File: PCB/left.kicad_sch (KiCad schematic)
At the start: 46 parts

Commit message: update footpint
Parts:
- D1, D10, D11, D12, D13, D14, D15, D16, D17, D18, D19, D2, D20, D21, D3, D4, D5, D6, D7, D8, D9: footprint kometa:Diode -> kometa:D_SOD323
- PS_L1: footprint kometa:MSK-12C02 -> kometa:SW_MSK-12C02
- PW_L1: footprint kometa:Battery -> kometa:J_Battery
- R_L1: footprint kometa:Reset -> kometa:SW_TS342A2P
- SM_L1: footprint kometa:SuperMini -> kometa:U_ProMicro_nRF52840
- SW1, SW10, SW11, SW12, SW13, SW14, SW15, SW16, SW17, SW18, SW19, SW2, SW20, SW21, SW3, SW4, SW5, SW6, SW7, SW8, SW9: footprint kometa:ChocV2 -> kometa:SW_Hotswap_Kailh_Choc_V1V2
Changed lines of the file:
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@@
 			)
 		)
-		(property "Footprint" "kometa:ChocV2"
+		(property "Footprint" "kometa:SW_Hotswap_Kailh_Choc_V1V2"
 			(at 79.756 105.41 0)
 			(effects
@@
 			)
 		)
-		(property "Footprint" "kometa:ChocV2"
+		(property "Footprint" "kometa:SW_Hotswap_Kailh_Choc_V1V2"
 			(at 136.906 105.41 0)
 			(effects
@@
 			)
 		)
-		(property "Footprint" "kometa:ChocV2"
+		(property "Footprint" "kometa:SW_Hotswap_Kailh_Choc_V1V2"
 			(at 41.656 86.36 0)
 			(effects
@@
 			)
 		)
-		(property "Footprint" "kometa:Diode"
+		(property "Footprint" "kometa:D_SOD323"
 			(at 138.176 102.362 0)
 			(effects
@@
 			)
 		)
-		(property "Footprint" "kometa:ChocV2"
+		(property "Footprint" "kometa:SW_Hotswap_Kailh_Choc_V1V2"
 			(at 136.906 86.36 0)
 			(effects
@@
 			)
 		)
-		(property "Footprint" "kometa:Diode"
+		(property "Footprint" "kometa:D_SOD323"
 			(at 61.976 83.312 0)
 			(effects
@@
 			)
 		)
-		(property "Footprint" "kometa:Battery"
+		(property "Footprint" "kometa:J_Battery"
 			(at 176.784 78.486 0)
 			(effects
@@
 			)
 		)
-		(property "Footprint" "kometa:Diode"
+		(property "Footprint" "kometa:D_SOD323"
 			(at 81.026 102.362 0)
 			(effects
@@
 			)
 		)
-		(property "Footprint" "kometa:ChocV2"
+		(property "Footprint" "kometa:SW_Hotswap_Kailh_Choc_V1V2"
 			(at 98.806 124.46 0)
 			(effects
@@
 			)
 		)
-		(property "Footprint" "kometa:ChocV2"
+		(property "Footprint" "kometa:SW_Hotswap_Kailh_Choc_V1V2"
 			(at 136.906 124.46 0)
 			(effects
@@
 			)
 		)
-		(property "Footprint" "kometa:ChocV2"
+		(property "Footprint" "kometa:SW_Hotswap_Kailh_Choc_V1V2"
 			(at 60.706 86.36 0)
 			(effects
@@
 			)
 		)
-		(property "Footprint" "kometa:ChocV2"
+		(property "Footprint" "kometa:SW_Hotswap_Kailh_Choc_V1V2"
 			(at 117.856 144.78 0)
 			(effects
@@
 			)
 		)
-		(property "Footprint" "kometa:Diode"
+		(property "Footprint" "kometa:D_SOD323"
 			(at 100.076 141.732 0)
 			(effects
@@
 			)
 		)
-		(property "Footprint" "kometa:ChocV2"
+		(property "Footprint" "kometa:SW_Hotswap_Kailh_Choc_V1V2"
 			(at 117.856 105.41 0)
 			(effects
@@
 			)
 		)
-		(property "Footprint" "kometa:ChocV2"
+		(property "Footprint" "kometa:SW_Hotswap_Kailh_Choc_V1V2"
 			(at 79.756 86.36 0)
 			(effects
@@
 			)
 		)
-		(property "Footprint" "kometa:Diode"
+		(property "Footprint" "kometa:D_SOD323"
 			(at 119.126 141.732 0)
 			(effects
@@
 			)
 		)
-		(property "Footprint" "kometa:Diode"
+		(property "Footprint" "kometa:D_SOD323"
 			(at 81.026 121.412 0)
 			(effects
@@
 			)
 		)
-		(property "Footprint" "kometa:Reset"
+		(property "Footprint" "kometa:SW_TS342A2P"
 			(at 185.42 102.87 0)
 			(effects
@@
 			)
 		)
-		(property "Footprint" "kometa:Diode"
+		(property "Footprint" "kometa:D_SOD323"
 			(at 81.026 83.312 0)
 			(effects
@@
 			)
 		)
-		(property "Footprint" "kometa:Diode"
+		(property "Footprint" "kometa:D_SOD323"
 			(at 119.126 102.362 0)
 			(effects
@@
 			)
 		)
-		(property "Footprint" "kometa:Diode"
+		(property "Footprint" "kometa:D_SOD323"
 			(at 138.176 121.412 0)
 			(effects
@@
 			)
 		)
-		(property "Footprint" "kometa:Diode"
+		(property "Footprint" "kometa:D_SOD323"
 			(at 42.926 83.312 0)
 			(effects
@@
 			)
 		)
-		(property "Footprint" "kometa:Diode"
+		(property "Footprint" "kometa:D_SOD323"
 			(at 42.926 121.412 0)
 			(effects
@@
 			)
 		)
-		(property "Footprint" "kometa:ChocV2"
+		(property "Footprint" "kometa:SW_Hotswap_Kailh_Choc_V1V2"
 			(at 117.856 86.36 0)
 			(effects
@@
 			)
 		)
-		(property "Footprint" "kometa:Diode"
+		(property "Footprint" "kometa:D_SOD323"
 			(at 119.126 121.412 0)
 			(effects
@@
 			)
 		)
-		(property "Footprint" "kometa:ChocV2"
+		(property "Footprint" "kometa:SW_Hotswap_Kailh_Choc_V1V2"
 			(at 41.656 124.46 0)
 			(effects
@@
 			)
 		)
-		(property "Footprint" "kometa:Diode"
+		(property "Footprint" "kometa:D_SOD323"
 			(at 138.176 83.312 0)
 			(effects
@@
 			)
 		)
-		(property "Footprint" "kometa:ChocV2"
+		(property "Footprint" "kometa:SW_Hotswap_Kailh_Choc_V1V2"
 			(at 60.706 124.46 0)
 			(effects
@@
 			)
 		)
-		(property "Footprint" "kometa:Diode"
+		(property "Footprint" "kometa:D_SOD323"
 			(at 61.976 102.362 0)
 			(effects
@@
 			)
 		)
-		(property "Footprint" "kometa:ChocV2"
+		(property "Footprint" "kometa:SW_Hotswap_Kailh_Choc_V1V2"
 			(at 98.806 86.36 0)
 			(effects
@@
 			)
 		)
-		(property "Footprint" "kometa:ChocV2"
+		(property "Footprint" "kometa:SW_Hotswap_Kailh_Choc_V1V2"
 			(at 117.856 124.46 0)
 			(effects
@@
 			)
 		)
-		(property "Footprint" "kometa:ChocV2"
+		(property "Footprint" "kometa:SW_Hotswap_Kailh_Choc_V1V2"
 			(at 98.806 144.78 0)
 			(effects
@@
 			)
 		)
-		(property "Footprint" "kometa:ChocV2"
+		(property "Footprint" "kometa:SW_Hotswap_Kailh_Choc_V1V2"
 			(at 41.656 105.41 0)
 			(effects
@@
 			)
 		)
-		(property "Footprint" "kometa:Diode"
+		(property "Footprint" "kometa:D_SOD323"
 			(at 138.176 141.732 0)
 			(effects
@@
 			)
 		)
-		(property "Footprint" "kometa:Diode"
+		(property "Footprint" "kometa:D_SOD323"
 			(at 119.126 83.312 0)
 			(effects
@@
 			)
 		)
-		(property "Footprint" "kometa:ChocV2"
+		(property "Footprint" "kometa:SW_Hotswap_Kailh_Choc_V1V2"
 			(at 60.706 105.41 0)
 			(effects
@@
 			)
 		)
-		(property "Footprint" "kometa:ChocV2"
+		(property "Footprint" "kometa:SW_Hotswap_Kailh_Choc_V1V2"
 			(at 98.806 105.41 0)
 			(effects
@@
 			)
 		)
-		(property "Footprint" "kometa:ChocV2"
+		(property "Footprint" "kometa:SW_Hotswap_Kailh_Choc_V1V2"
 			(at 79.756 124.46 0)
 			(effects
@@
 			)
 		)
-		(property "Footprint" "kometa:SuperMini"
+		(property "Footprint" "kometa:U_ProMicro_nRF52840"
 			(at 241.3 109.728 0)
 			(effects
@@
 			)
 		)
-		(property "Footprint" "kometa:Diode"
+		(property "Footprint" "kometa:D_SOD323"
 			(at 61.976 121.412 0)
 			(effects
@@
 			)
 		)
-		(property "Footprint" "kometa:MSK-12C02"
+		(property "Footprint" "kometa:SW_MSK-12C02"
 			(at 186.944 80.264 0)
 			(effects
@@
 			)
 		)
-		(property "Footprint" "kometa:Diode"
+		(property "Footprint" "kometa:D_SOD323"
 			(at 100.076 83.312 0)
 			(effects
@@
 			)
 		)
-		(property "Footprint" "kometa:ChocV2"
+		(property "Footprint" "kometa:SW_Hotswap_Kailh_Choc_V1V2"
 			(at 136.906 144.78 0)
 			(effects
@@
 			)
 		)
-		(property "Footprint" "kometa:Diode"
+		(property "Footprint" "kometa:D_SOD323"
 			(at 100.076 121.412 0)
 			(effects
@@
 			)
 		)
-		(property "Footprint" "kometa:Diode"
+		(property "Footprint" "kometa:D_SOD323"
 			(at 42.926 102.362 0)
 			(effects
@@
 			)
 		)
-		(property "Footprint" "kometa:Diode"
+		(property "Footprint" "kometa:D_SOD323"
 			(at 100.076 102.362 0)
 			(effects

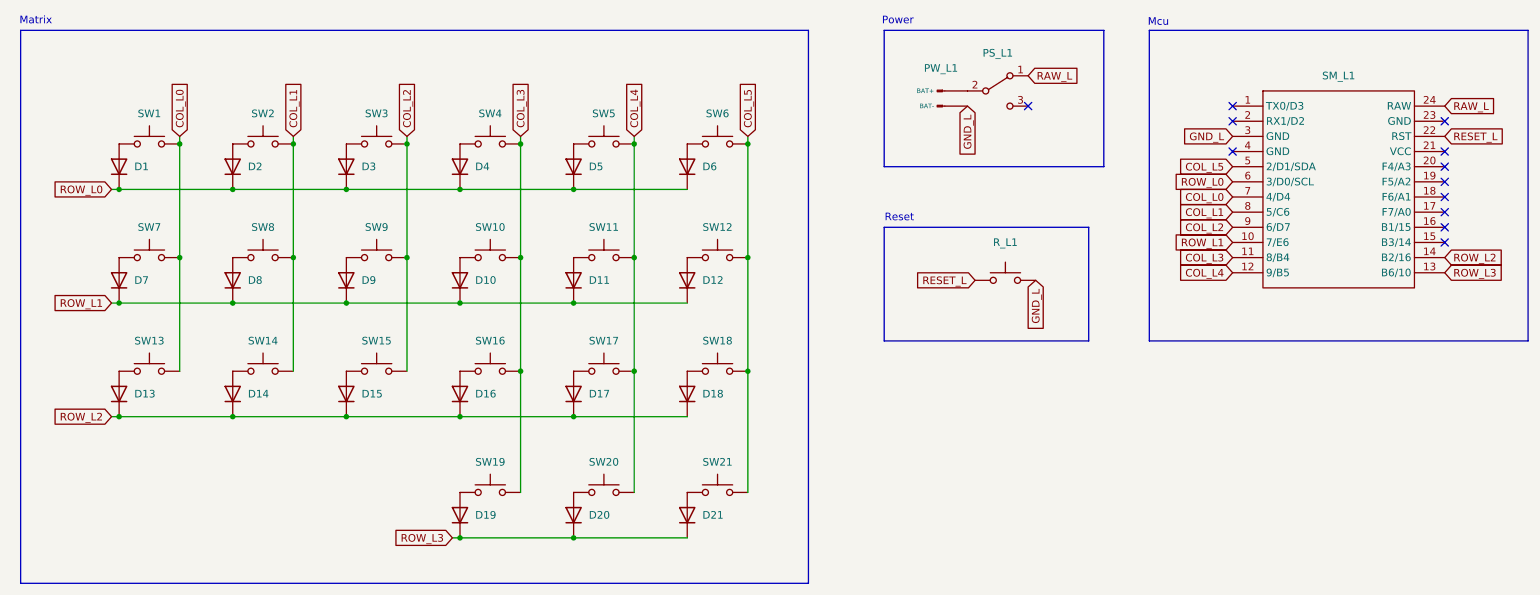
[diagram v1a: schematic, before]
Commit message: add led sh and pretty
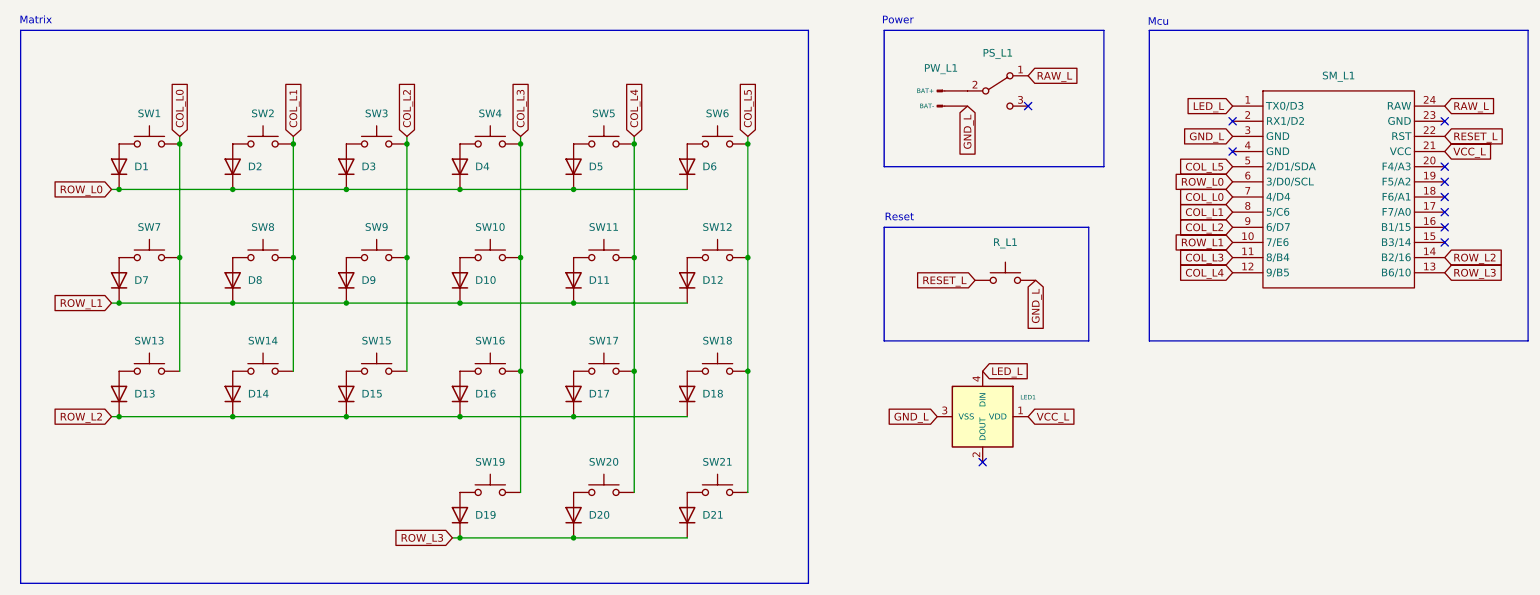
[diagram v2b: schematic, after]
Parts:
- added LED1: ~, kometa:YS-SK6812MINI-E, symbol kometa:YS-SK6812MINI-E
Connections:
- net GND_L: now also LED1.3 (VSS)
- net LED_L: now reaches SM_L1.1 (TX0/D3)
- net LED_L: now also LED1.4 (DIN)
- net VCC_L: now reaches SM_L1.21 (VCC)
- net VCC_L: now also LED1.1 (VDD)
- no-connect marks 12 -> 11
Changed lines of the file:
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@@
 	)
 	(no_connect
-		(at 223.52 73.66)
-	)
-	(no_connect
 		(at 223.52 76.2)
 	)
@@
 	)
 	(no_connect
-		(at 189.23 73.66)
+		(at 181.61 133.35)
 	)
 	(no_connect
-		(at 259.08 88.9)
+		(at 189.23 73.66)
 	)
 	(no_connect
-		(at 259.08 81.28)
+		(at 259.08 88.9)
 	)
 	(no_connect
@@
 		)
 	)
+	(global_label "VCC_L"
+		(shape input)
+		(at 189.23 125.73 0)
+		(fields_autoplaced yes)
+		(effects
+			(font
+				(size 1.27 1.27)
+			)
+			(justify left)
+		)
+		(property "Intersheetrefs" "${INTERSHEET_REFS}"
+			(at 197.8395 125.73 0)
+			(effects
+				(font
+					(size 1.27 1.27)
+				)
+				(justify left)
+				(hide yes)
+			)
+		)
+	)
 	(global_label "COL_L4"
 		(shape input)
@@
 		)
 	)
+	(global_label "LED_L"
+		(shape input)
+		(at 223.52 73.66 180)
+		(fields_autoplaced yes)
+		(effects
+			(font
+				(size 1.27 1.27)
+			)
+			(justify right)
+		)
+		(property "Intersheetrefs" "${INTERSHEET_REFS}"
+			(at 215.092 73.66 0)
+			(effects
+				(font
+					(size 1.27 1.27)
+				)
+				(justify right)
+				(hide yes)
+			)
+		)
+	)
 	(global_label "ROW_L1"
 		(shape input)
@@
 		)
 	)
+	(global_label "GND_L"
+		(shape input)
+		(at 173.99 125.73 180)
+		(fields_autoplaced yes)
+		(effects
+			(font
+				(size 1.27 1.27)
+			)
+			(justify right)
+		)
+		(property "Intersheetrefs" "${INTERSHEET_REFS}"
+			(at 165.1386 125.73 0)
+			(effects
+				(font
+					(size 1.27 1.27)
+				)
+				(justify right)
+				(hide yes)
+			)
+		)
+	)
 	(global_label "COL_L0"
 		(shape input)
@@
 		)
 	)
+	(global_label "LED_L"
+		(shape input)
+		(at 181.61 118.11 0)
+		(fields_autoplaced yes)
+		(effects
+			(font
+				(size 1.27 1.27)
+			)
+			(justify left)
+		)
+		(property "Intersheetrefs" "${INTERSHEET_REFS}"
+			(at 190.038 118.11 0)
+			(effects
+				(font
+					(size 1.27 1.27)
+				)
+				(justify left)
+				(hide yes)
+			)
+		)
+	)
 	(global_label "COL_L5"
 		(shape input)
@@
 		)
 	)
+	(global_label "VCC_L"
+		(shape input)
+		(at 259.08 81.28 0)
+		(fields_autoplaced yes)
+		(effects
+			(font
+				(size 1.27 1.27)
+			)
+			(justify left)
+		)
+		(property "Intersheetrefs" "${INTERSHEET_REFS}"
+			(at 267.6895 81.28 0)
+			(effects
+				(font
+					(size 1.27 1.27)
+				)
+				(justify left)
+				(hide yes)
+			)
+		)
+	)
 	(global_label "RESET_L"
 		(shape input)
@@
 					(unit 1)
 				)
+			)
+		)
+	)
+	(symbol
+		(lib_id "kometa:YS-SK6812MINI-E")
+		(at 181.61 125.73 0)
+		(unit 1)
+		(exclude_from_sim no)
+		(in_bom yes)
+		(on_board yes)
+		(dnp no)
+		(fields_autoplaced yes)
+		(property "Reference" "LED1"
+			(at 189.23 122.4849 0)
+			(effects
+				(font
+					(size 0.7366 0.7366)
+				)
+			)
+		)
+		(property "Value" "~"
+			(at 188.214 132.08 0)
+			(effects
+				(font
+					(size 0.7366 0.7366)
+				)
+				(hide yes)
+			)
+		)
+		(property "Footprint" "kometa:YS-SK6812MINI-E"
+			(at 184.15 132.08 0)
+			(effects
+				(font
+					(size 1.27 1.27)
+				)
+				(hide yes)
+			)
+		)
+		(property "Datasheet" ""
+			(at 184.15 132.08 0)
+			(effects
+				(font
+					(size 1.27 1.27)
+				)
+				(hide yes)
+			)
+		)
+		(property "Description" ""
+			(at 181.61 125.73 0)
+			(effects
+				(font
+					(size 1.27 1.27)
+				)
+				(hide yes)
+			)
+		)
+		(pin "3"
+		)
+		(pin "4"
+		)
+		(pin "1"
+		)
+		(pin "2"
+		)
+		(instances
+			(project ""
+				(path "/87d0d44c-3cdf-4c1b-91f4-ef0852a5e1e5/56666e1e-9460-4275-af0a-60c0fca684c8"
+					(reference "LED1")
+					(unit 1)
+				)

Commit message: Experimental KS27/KS33 support
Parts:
- SW1, SW10, SW11, SW12, SW13, SW14, SW15, SW16, SW17, SW18, SW19, SW2, SW20, SW21, SW3, SW4, SW5, SW6, SW7, SW8, SW9: footprint kometa:SW_Hotswap_Kailh_Choc_V1V2 -> kometa:SW_Hotswap_Kailh_Choc_V1V2_with_KS27_KS33
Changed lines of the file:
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@@
 			)
 		)
-		(property "Footprint" "kometa:SW_Hotswap_Kailh_Choc_V1V2"
+		(property "Footprint" "kometa:SW_Hotswap_Kailh_Choc_V1V2_with_KS27_KS33"
 			(at 79.756 105.41 0)
 			(effects
@@
 			)
 		)
-		(property "Footprint" "kometa:SW_Hotswap_Kailh_Choc_V1V2"
+		(property "Footprint" "kometa:SW_Hotswap_Kailh_Choc_V1V2_with_KS27_KS33"
 			(at 136.906 105.41 0)
 			(effects
@@
 			)
 		)
-		(property "Footprint" "kometa:SW_Hotswap_Kailh_Choc_V1V2"
+		(property "Footprint" "kometa:SW_Hotswap_Kailh_Choc_V1V2_with_KS27_KS33"
 			(at 41.656 86.36 0)
 			(effects
@@
 			)
 		)
-		(property "Footprint" "kometa:SW_Hotswap_Kailh_Choc_V1V2"
+		(property "Footprint" "kometa:SW_Hotswap_Kailh_Choc_V1V2_with_KS27_KS33"
 			(at 136.906 86.36 0)
 			(effects
@@
 			)
 		)
-		(property "Footprint" "kometa:SW_Hotswap_Kailh_Choc_V1V2"
+		(property "Footprint" "kometa:SW_Hotswap_Kailh_Choc_V1V2_with_KS27_KS33"
 			(at 98.806 124.46 0)
 			(effects
@@
 			)
 		)
-		(property "Footprint" "kometa:SW_Hotswap_Kailh_Choc_V1V2"
+		(property "Footprint" "kometa:SW_Hotswap_Kailh_Choc_V1V2_with_KS27_KS33"
 			(at 136.906 124.46 0)
 			(effects
@@
 			)
 		)
-		(property "Footprint" "kometa:SW_Hotswap_Kailh_Choc_V1V2"
+		(property "Footprint" "kometa:SW_Hotswap_Kailh_Choc_V1V2_with_KS27_KS33"
 			(at 60.706 86.36 0)
 			(effects
@@
 			)
 		)
-		(property "Footprint" "kometa:SW_Hotswap_Kailh_Choc_V1V2"
+		(property "Footprint" "kometa:SW_Hotswap_Kailh_Choc_V1V2_with_KS27_KS33"
 			(at 117.856 144.78 0)
 			(effects
@@
 			)
 		)
-		(property "Footprint" "kometa:SW_Hotswap_Kailh_Choc_V1V2"
+		(property "Footprint" "kometa:SW_Hotswap_Kailh_Choc_V1V2_with_KS27_KS33"
 			(at 117.856 105.41 0)
 			(effects
@@
 			)
 		)
-		(property "Footprint" "kometa:SW_Hotswap_Kailh_Choc_V1V2"
+		(property "Footprint" "kometa:SW_Hotswap_Kailh_Choc_V1V2_with_KS27_KS33"
 			(at 79.756 86.36 0)
 			(effects
@@
 			)
 		)
-		(property "Footprint" "kometa:SW_Hotswap_Kailh_Choc_V1V2"
+		(property "Footprint" "kometa:SW_Hotswap_Kailh_Choc_V1V2_with_KS27_KS33"
 			(at 117.856 86.36 0)
 			(effects
@@
 			)
 		)
-		(property "Footprint" "kometa:SW_Hotswap_Kailh_Choc_V1V2"
+		(property "Footprint" "kometa:SW_Hotswap_Kailh_Choc_V1V2_with_KS27_KS33"
 			(at 41.656 124.46 0)
 			(effects
@@
 			)
 		)
-		(property "Footprint" "kometa:SW_Hotswap_Kailh_Choc_V1V2"
+		(property "Footprint" "kometa:SW_Hotswap_Kailh_Choc_V1V2_with_KS27_KS33"
 			(at 60.706 124.46 0)
 			(effects
@@
 			)
 		)
-		(property "Footprint" "kometa:SW_Hotswap_Kailh_Choc_V1V2"
+		(property "Footprint" "kometa:SW_Hotswap_Kailh_Choc_V1V2_with_KS27_KS33"
 			(at 98.806 86.36 0)
 			(effects
@@
 			)
 		)
-		(property "Footprint" "kometa:SW_Hotswap_Kailh_Choc_V1V2"
+		(property "Footprint" "kometa:SW_Hotswap_Kailh_Choc_V1V2_with_KS27_KS33"
 			(at 117.856 124.46 0)
 			(effects
@@
 			)
 		)
-		(property "Footprint" "kometa:SW_Hotswap_Kailh_Choc_V1V2"
+		(property "Footprint" "kometa:SW_Hotswap_Kailh_Choc_V1V2_with_KS27_KS33"
 			(at 98.806 144.78 0)
 			(effects
@@
 			)
 		)
-		(property "Footprint" "kometa:SW_Hotswap_Kailh_Choc_V1V2"
+		(property "Footprint" "kometa:SW_Hotswap_Kailh_Choc_V1V2_with_KS27_KS33"
 			(at 41.656 105.41 0)
 			(effects
@@
 			)
 		)
-		(property "Footprint" "kometa:SW_Hotswap_Kailh_Choc_V1V2"
+		(property "Footprint" "kometa:SW_Hotswap_Kailh_Choc_V1V2_with_KS27_KS33"
 			(at 60.706 105.41 0)
 			(effects
@@
 			)
 		)
-		(property "Footprint" "kometa:SW_Hotswap_Kailh_Choc_V1V2"
+		(property "Footprint" "kometa:SW_Hotswap_Kailh_Choc_V1V2_with_KS27_KS33"
 			(at 98.806 105.41 0)
 			(effects
@@
 			)
 		)
-		(property "Footprint" "kometa:SW_Hotswap_Kailh_Choc_V1V2"
+		(property "Footprint" "kometa:SW_Hotswap_Kailh_Choc_V1V2_with_KS27_KS33"
 			(at 79.756 124.46 0)
 			(effects
@@
 			)
 		)
-		(property "Footprint" "kometa:SW_Hotswap_Kailh_Choc_V1V2"
+		(property "Footprint" "kometa:SW_Hotswap_Kailh_Choc_V1V2_with_KS27_KS33"
 			(at 136.906 144.78 0)
 			(effects
